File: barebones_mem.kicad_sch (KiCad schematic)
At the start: 0 parts

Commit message: routed the two 64Gb LPDDR4x RAM chips
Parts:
- added C128, C132: 47uF, Capacitor_SMD:C_0603_1608Metric, symbol Device:C
- added D15: TPD1E05U06DPYR, TPD1E05U06DPYR:DIO_TPD1E05U06DPYR, symbol TPD1E05U06DPYR:TPD1E05U06DPYR
- added Q4: MMBT3904, MMBT3904:P200_SOT-23, symbol MMBT3904:MMBT3904
- added R166, R167, R169: 10k, Resistor_SMD:R_0603_1608Metric, symbol Device:R
- added R168: 22R, Resistor_SMD:R_0603_1608Metric, symbol Device:R
- added TP5: RESETB, TestPoint:TestPoint_Pad_D1.5mm, symbol Connector:TestPoint
- added TP6: GND, TestPoint:TestPoint_Pad_D1.5mm, symbol Connector:TestPoint
- added U49: W25Q256JWEIQ, barebones:WSON-8_L8.0-W6.0-P1.27-TL-EP-1, symbol W25Q256JWEIQ:W25Q256JWEIQ_C2980994
- added U50: PCF85063ATL/1,118, barebones:10-DFN_2.6X2.6_, symbol PCF85063ATL_1_118:PCF85063ATL_1_118
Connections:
- new net: D15.2 (GND), Q4.1 (B), R169.2
- new net: R169.1, TP5.1
- new net: Q4.3 (C), R168.2
- new net FSPI-CLK: R168.1, U49.6 (CLK)
- new net FSPI-CS0: U49.1 (~{CS})
- new net FSPI-D0: U49.5 (DI(IO0))
- new net FSPI-D1: U49.2 (DO(IO1))
- new net FSPI-D2: R166.2, U49.3 (WP#(IO2))
- new net FSPI-D3: R167.2, U49.7 (~{HOLDor}/RESET#(IO3))
- new net GND: C128.1, C132.1, D15.1 (I/O), Q4.2 (E), U49.4 (GND), U49.9 (EP)
- new net VCC_1V8_S3: C128.2, C132.2, R166.1, R167.1, TP6.1, U49.8 (VCC)
- new net VSS: U50.11 (VSS), U50.5 (VSS)

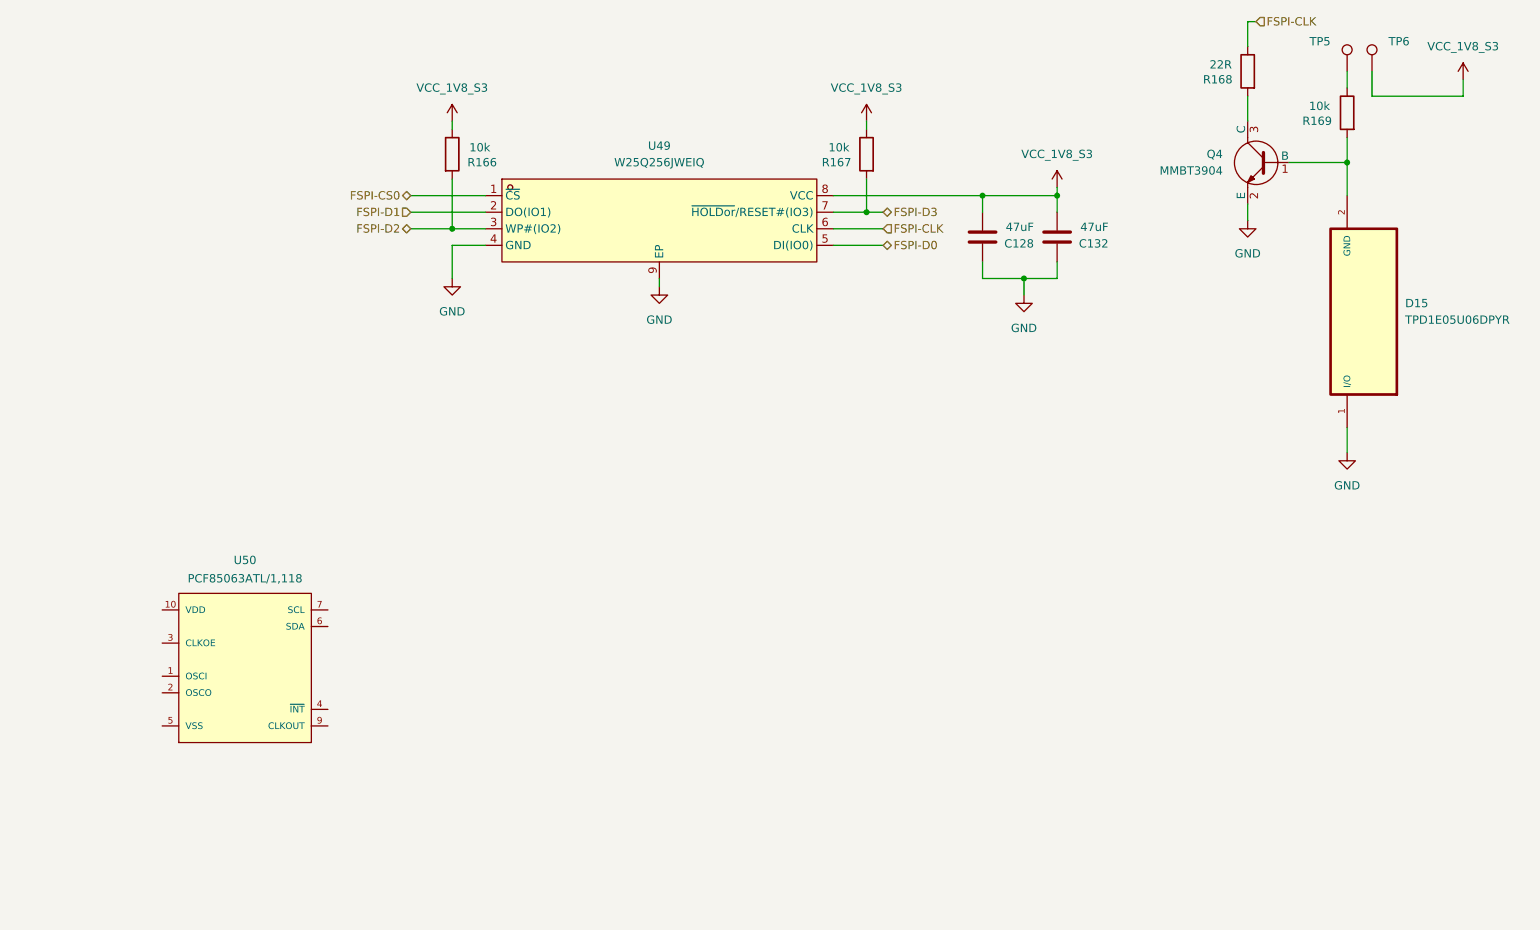
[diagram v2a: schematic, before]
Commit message: added the STM32L433RCT6 to act as the embedded controller
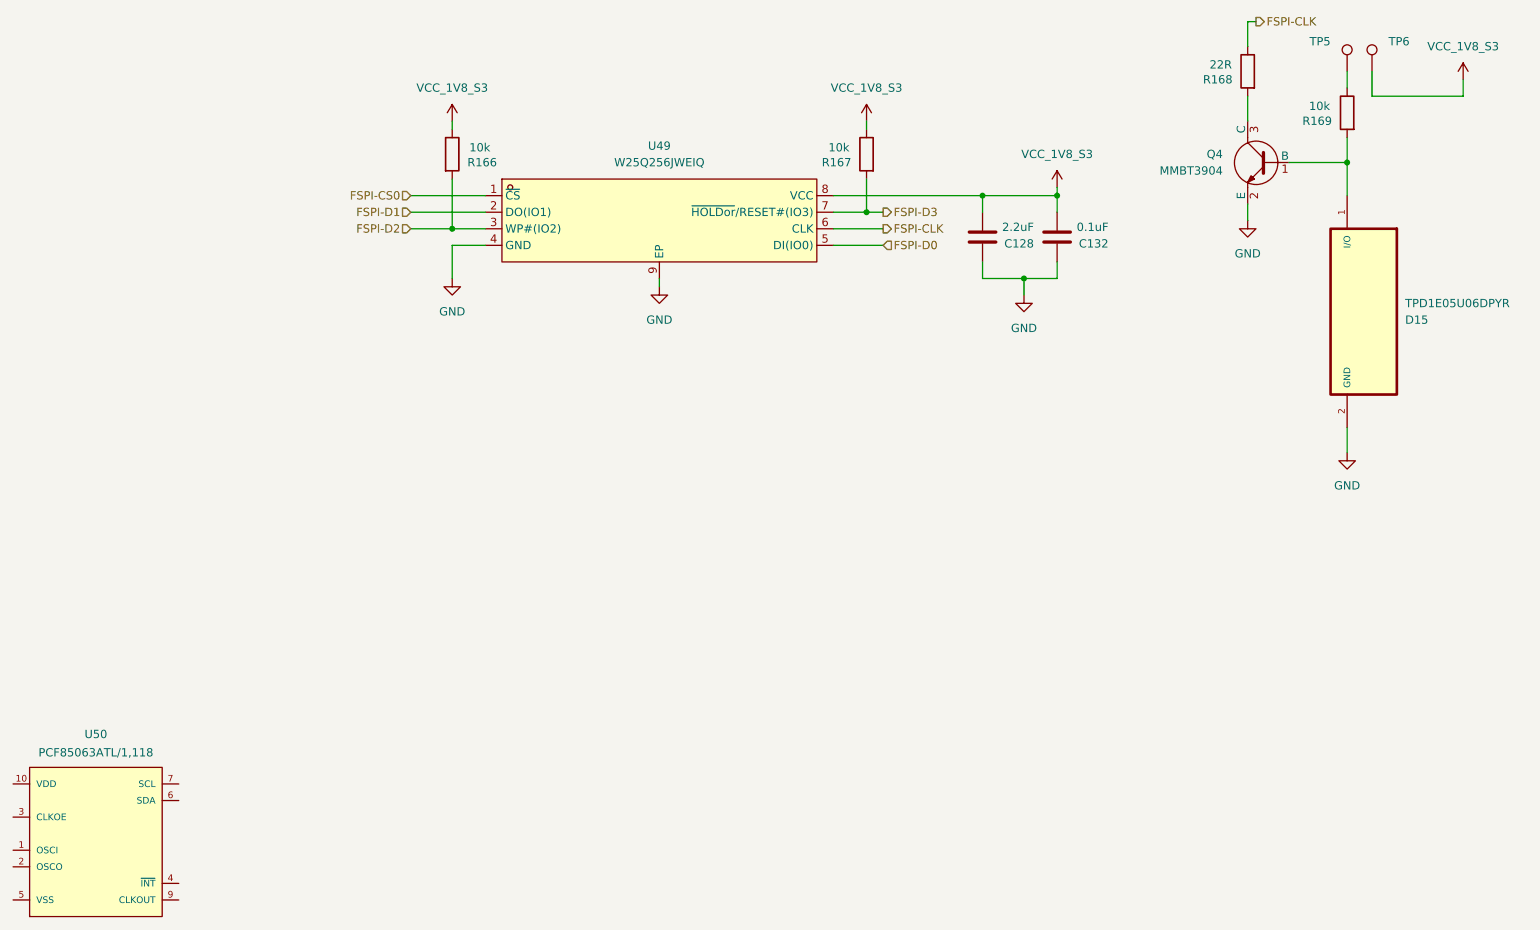
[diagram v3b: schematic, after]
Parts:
- C128: value 47uF -> 2.2uF
- C132: value 47uF -> 0.1uF
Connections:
- net GND: now also D15.2 (GND); no longer D15.1 (I/O)
- net at Q4.1 (B), R169.2: now also D15.1 (I/O); no longer D15.2 (GND)
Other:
- moved on the sheet: U50
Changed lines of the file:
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@@
 	)
 	(hierarchical_label "FSPI-CLK"
-		(shape input)
+		(shape output)
 		(at 184.15 53.34 0)
 		(effects
@@
 	)
 	(hierarchical_label "FSPI-D0"
-		(shape bidirectional)
+		(shape input)
 		(at 184.15 55.88 0)
 		(effects
@@
 	)
 	(hierarchical_label "FSPI-CLK"
-		(shape input)
+		(shape output)
 		(at 241.3 21.59 0)
 		(effects
@@
 	)
 	(hierarchical_label "FSPI-D3"
-		(shape bidirectional)
+		(shape output)
 		(at 184.15 50.8 0)
 		(effects
@@
 	)
 	(hierarchical_label "FSPI-CS0"
-		(shape bidirectional)
+		(shape input)
 		(at 111.76 48.26 180)
 		(effects
@@
 	)
 	(hierarchical_label "FSPI-D2"
-		(shape bidirectional)
+		(shape input)
 		(at 111.76 53.34 180)
 		(effects
@@
 		(lib_id "TPD1E05U06DPYR:TPD1E05U06DPYR")
 		(at 257.81 66.04 90)
-		(unit 1)
-		(body_style 1)
-		(exclude_from_sim no)
-		(in_bom yes)
-		(on_board yes)
-		(in_pos_files yes)
-		(dnp no)
-		(fields_autoplaced yes)
+		(mirror x)
+		(unit 1)
+		(body_style 1)
+		(exclude_from_sim no)
+		(in_bom yes)
+		(on_board yes)
+		(in_pos_files yes)
+		(dnp no)
 		(property "Reference" "D15"
-			(at 264.16 64.7699 90)
+			(at 264.16 67.3101 90)
 			(show_name no)
 			(do_not_autoplace no)
@@
 		)
 		(property "Value" "TPD1E05U06DPYR"
-			(at 264.16 67.3099 90)
+			(at 264.16 64.7701 90)
 			(show_name no)
 			(do_not_autoplace no)
@@
 			)
 		)
-		(property "Value" "47uF"
+		(property "Value" "2.2uF"
 			(at 207.264 53.086 0)
 			(show_name no)
@@
 			)
 		)
-		(property "Value" "47uF"
+		(property "Value" "0.1uF"
 			(at 218.694 53.086 0)
 			(show_name no)
@@
 	(symbol
 		(lib_id "PCF85063ATL_1_118:PCF85063ATL_1_118")
-		(at 86.36 119.38 0)
+		(at 63.5 146.05 0)
 		(unit 1)
 		(body_style 1)
@@
 		(dnp no)
 		(property "Reference" "U50"
-			(at 86.36 104.14 0)
+			(at 63.5 130.81 0)
 			(show_name no)
 			(do_not_autoplace no)
@@
 		)
 		(property "Value" "PCF85063ATL/1,118"
-			(at 86.36 107.696 0)
+			(at 63.5 134.366 0)
 			(show_name no)
 			(do_not_autoplace no)
@@
 		)
 		(property "Footprint" "barebones:10-DFN_2.6X2.6_"
-			(at 86.36 119.38 0)
+			(at 63.5 146.05 0)
 			(hide yes)
 			(show_name no)
@@
 		)
 		(property "Datasheet" ""
-			(at 86.36 119.38 0)
+			(at 63.5 146.05 0)
 			(hide yes)
 			(show_name no)
@@
 		)
 		(property "Description" "Real Time Clock (RTC) IC Clock/Calendar - I²C, 2-Wire Serial 10-XFDFN Exposed Pad"
-			(at 86.36 119.38 0)
+			(at 63.5 146.05 0)
 			(hide yes)
 			(show_name no)
@@
 		)
 		(property "MF" "NXP USA"
-			(at 86.36 119.38 0)
+			(at 63.5 146.05 0)
 			(hide yes)
 			(show_name no)
@@
 		)
 		(property "Package" "DFN-10 NXP Semiconductors"
-			(at 86.36 119.38 0)
+			(at 63.5 146.05 0)
 			(hide yes)
 			(show_name no)
@@
 		)
 		(property "Price" "None"
-			(at 86.36 119.38 0)
+			(at 63.5 146.05 0)
 			(hide yes)
 			(show_name no)
@@
 		)
 		(property "Check_prices" "https://www.snapeda.com/parts/PCF85063ATL/1,118/NXP+Semiconductors/view-part/?ref=eda"
-			(at 86.36 119.38 0)
+			(at 63.5 146.05 0)
 			(hide yes)
 			(show_name no)
@@
 		)
 		(property "SnapEDA_Link" "https://www.snapeda.com/parts/PCF85063ATL/1,118/NXP+Semiconductors/view-part/?ref=snap"
-			(at 86.36 119.38 0)
+			(at 63.5 146.05 0)
 			(hide yes)
 			(show_name no)
@@
 		)
 		(property "PROD_ID" "IC-15415"
-			(at 86.36 119.38 0)
+			(at 63.5 146.05 0)
 			(hide yes)
 			(show_name no)
@@
 		)
 		(property "Availability" "In Stock"
-			(at 86.36 119.38 0)
+			(at 63.5 146.05 0)
 			(hide yes)
 			(show_name no)
@@
 		)
 		(property "MP" "PCF85063ATL/1,118"
-			(at 86.36 119.38 0)
-			(hide yes)
-			(show_name no)
+			(at 63.5 146.05 0)
+			(hide yes)
+			(show_name no)

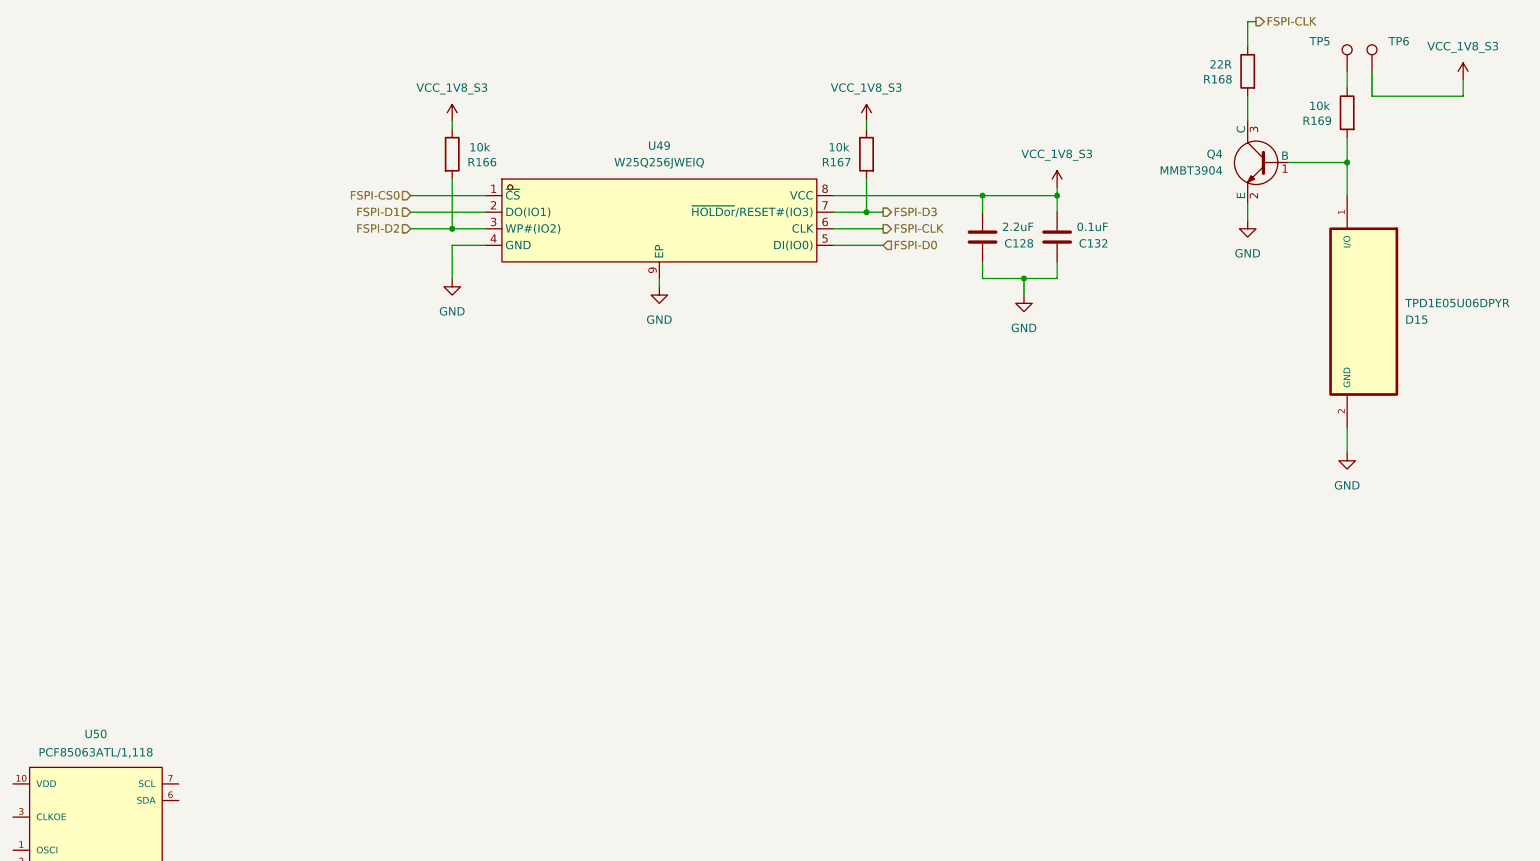
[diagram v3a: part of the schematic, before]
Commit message: added the display connector and its 12V power supply
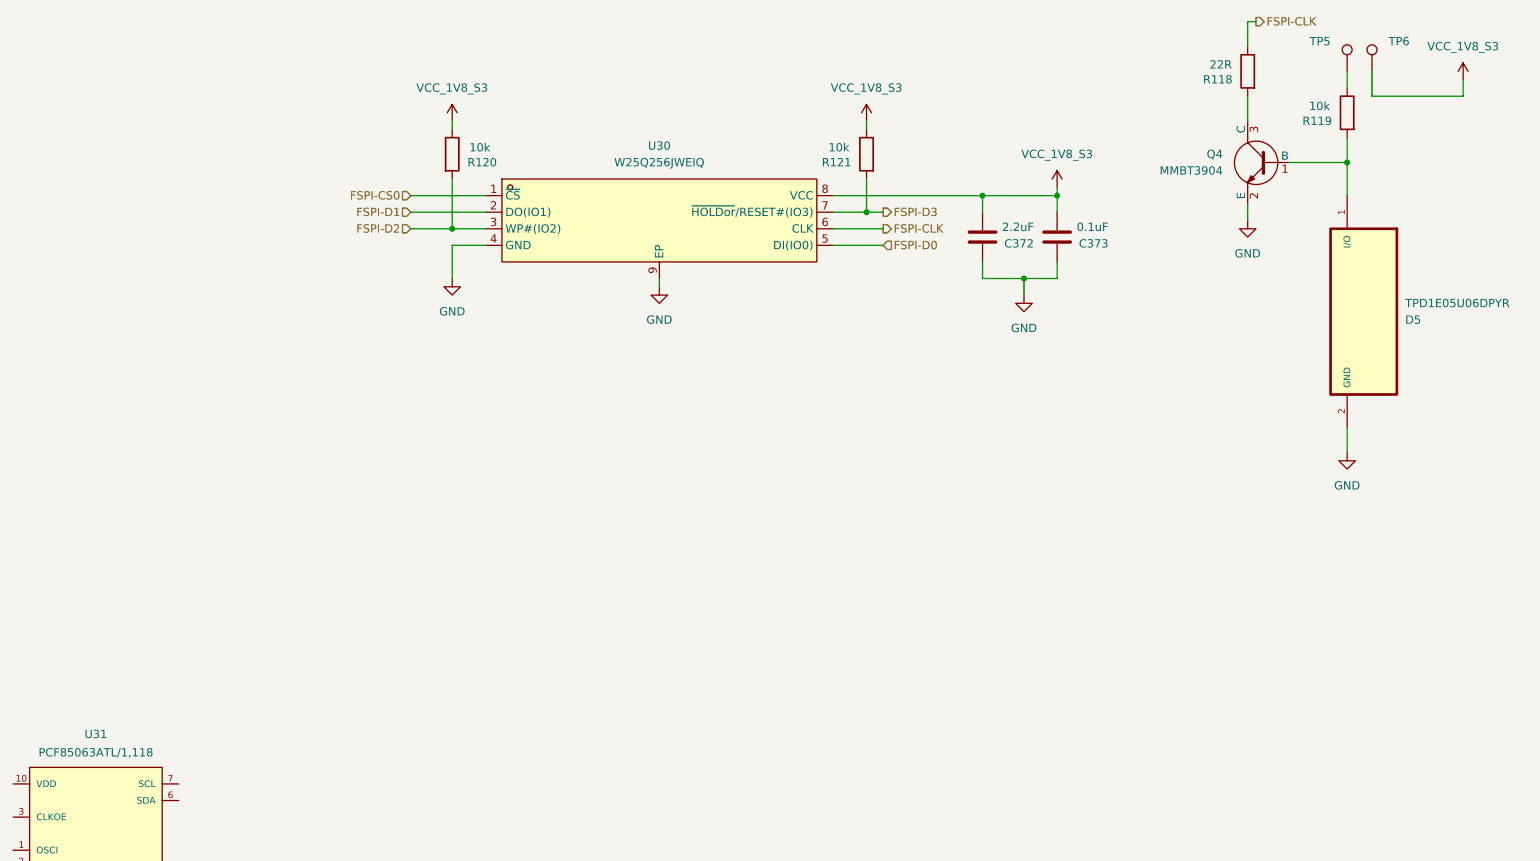
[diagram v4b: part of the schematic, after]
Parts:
- renumbered C128 to C372, C132 to C373, D15 to D5, R168 to R118, R169 to R119, R166 to R120, R167 to R121, U49 to U30, U50 to U31
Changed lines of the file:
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@@
 		(dnp no)
 		(fields_autoplaced yes)
-		(property "Reference" "#PWR0389"
+		(property "Reference" "#PWR0334"
 			(at 118.11 67.31 0)
 			(hide yes)
@@
 			(project "barebones"
 				(path "/55e8bb80-206a-472b-ac89-6555b6c3d282/10a7f033-abc9-48da-a7a0-2d26902a94e5"
-					(reference "#PWR0389")
+					(reference "#PWR0334")
 					(unit 1)
 				)
@@
 		(dnp no)
 		(fields_autoplaced yes)
-		(property "Reference" "#PWR0394"
+		(property "Reference" "#PWR0329"
 			(at 273.05 34.29 0)
 			(hide yes)
@@
 			(project "barebones"
 				(path "/55e8bb80-206a-472b-ac89-6555b6c3d282/10a7f033-abc9-48da-a7a0-2d26902a94e5"
-					(reference "#PWR0394")
+					(reference "#PWR0329")
 					(unit 1)
 				)
@@
 		(in_pos_files yes)
 		(dnp no)
-		(property "Reference" "D15"
+		(property "Reference" "D5"
 			(at 264.16 67.3101 90)
 			(show_name no)
@@
 			(project "barebones"
 				(path "/55e8bb80-206a-472b-ac89-6555b6c3d282/10a7f033-abc9-48da-a7a0-2d26902a94e5"
-					(reference "D15")
+					(reference "D5")
 					(unit 1)
 				)
@@
 		(in_pos_files yes)
 		(dnp no)
-		(property "Reference" "R169"
+		(property "Reference" "R119"
 			(at 248.412 36.83 0)
 			(show_name no)
@@
 			(project "barebones"
 				(path "/55e8bb80-206a-472b-ac89-6555b6c3d282/10a7f033-abc9-48da-a7a0-2d26902a94e5"
-					(reference "R169")
+					(reference "R119")
 					(unit 1)
 				)
@@
 		(in_pos_files yes)
 		(dnp no)
-		(property "Reference" "C128"
+		(property "Reference" "C372"
 			(at 207.264 55.626 0)
 			(show_name no)
@@
 			(project "barebones"
 				(path "/55e8bb80-206a-472b-ac89-6555b6c3d282/10a7f033-abc9-48da-a7a0-2d26902a94e5"
-					(reference "C128")
+					(reference "C372")
 					(unit 1)
 				)
@@
 		(dnp no)
 		(fields_autoplaced yes)
-		(property "Reference" "#PWR0391"
+		(property "Reference" "#PWR0336"
 			(at 205.74 69.85 0)
 			(hide yes)
@@
 			(project "barebones"
 				(path "/55e8bb80-206a-472b-ac89-6555b6c3d282/10a7f033-abc9-48da-a7a0-2d26902a94e5"
-					(reference "#PWR0391")
+					(reference "#PWR0336")
 					(unit 1)
 				)
@@
 		(dnp no)
 		(fields_autoplaced yes)
-		(property "Reference" "#PWR0387"
+		(property "Reference" "#PWR0332"
 			(at 210.82 50.8 0)
 			(hide yes)
@@
 			(project "barebones"
 				(path "/55e8bb80-206a-472b-ac89-6555b6c3d282/10a7f033-abc9-48da-a7a0-2d26902a94e5"
-					(reference "#PWR0387")
+					(reference "#PWR0332")
 					(unit 1)
 				)
@@
 		(in_pos_files yes)
 		(dnp no)
-		(property "Reference" "C132"
+		(property "Reference" "C373"
 			(at 218.694 55.626 0)
 			(show_name no)
@@
 			(project "barebones"
 				(path "/55e8bb80-206a-472b-ac89-6555b6c3d282/10a7f033-abc9-48da-a7a0-2d26902a94e5"
-					(reference "C132")
+					(reference "C373")
 					(unit 1)
 				)
@@
 		(dnp no)
 		(fields_autoplaced yes)
-		(property "Reference" "#PWR0393"
+		(property "Reference" "#PWR0333"
 			(at 240.03 58.42 0)
 			(hide yes)
@@
 			(project "barebones"
 				(path "/55e8bb80-206a-472b-ac89-6555b6c3d282/10a7f033-abc9-48da-a7a0-2d26902a94e5"
-					(reference "#PWR0393")
+					(reference "#PWR0333")
 					(unit 1)
 				)
@@
 		(dnp no)
 		(fields_autoplaced yes)
-		(property "Reference" "#PWR0386"
+		(property "Reference" "#PWR0330"
 			(at 118.11 40.64 0)
 			(hide yes)
@@
 			(project "barebones"
 				(path "/55e8bb80-206a-472b-ac89-6555b6c3d282/10a7f033-abc9-48da-a7a0-2d26902a94e5"
-					(reference "#PWR0386")
+					(reference "#PWR0330")
 					(unit 1)
 				)
@@
 		(in_pos_files yes)
 		(dnp no)
-		(property "Reference" "R168"
+		(property "Reference" "R118"
 			(at 233.172 30.48 0)
 			(show_name no)
@@
 			(project "barebones"
 				(path "/55e8bb80-206a-472b-ac89-6555b6c3d282/10a7f033-abc9-48da-a7a0-2d26902a94e5"
-					(reference "R168")
+					(reference "R118")
 					(unit 1)
 				)
@@
 		(dnp no)
 		(fields_autoplaced yes)
-		(property "Reference" "U49"
+		(property "Reference" "U30"
 			(at 149.86 40.64 0)
 			(show_name no)
@@
 			(project "barebones"
 				(path "/55e8bb80-206a-472b-ac89-6555b6c3d282/10a7f033-abc9-48da-a7a0-2d26902a94e5"
-					(reference "U49")
+					(reference "U30")
 					(unit 1)
 				)
@@
 		(dnp no)
 		(fields_autoplaced yes)
-		(property "Reference" "#PWR0392"
+		(property "Reference" "#PWR0337"
 			(at 255.27 93.98 0)
 			(hide yes)
@@
 			(project "barebones"
 				(path "/55e8bb80-206a-472b-ac89-6555b6c3d282/10a7f033-abc9-48da-a7a0-2d26902a94e5"
-					(reference "#PWR0392")
+					(reference "#PWR0337")
 					(unit 1)
 				)
@@
 		(in_pos_files yes)
 		(dnp no)
-		(property "Reference" "R167"
+		(property "Reference" "R121"
 			(at 174.752 43.18 0)
 			(show_name no)
@@
 			(project "barebones"
 				(path "/55e8bb80-206a-472b-ac89-6555b6c3d282/10a7f033-abc9-48da-a7a0-2d26902a94e5"
-					(reference "R167")
+					(reference "R121")
 					(unit 1)
 				)
@@
 		(dnp no)
 		(fields_autoplaced yes)
-		(property "Reference" "#PWR0390"
+		(property "Reference" "#PWR0335"
 			(at 149.86 68.58 0)
 			(hide yes)
@@
 			(project "barebones"
 				(path "/55e8bb80-206a-472b-ac89-6555b6c3d282/10a7f033-abc9-48da-a7a0-2d26902a94e5"
-					(reference "#PWR0390")
+					(reference "#PWR0335")
 					(unit 1)
 				)
@@
 		(in_pos_files yes)
 		(dnp no)
-		(property "Reference" "R166"
+		(property "Reference" "R120"
 			(at 124.968 43.18 0)
 			(show_name no)
@@
 			(project "barebones"
 				(path "/55e8bb80-206a-472b-ac89-6555b6c3d282/10a7f033-abc9-48da-a7a0-2d26902a94e5"
-					(reference "R166")
+					(reference "R120")
 					(unit 1)
 				)
@@
 		(dnp no)
 		(fields_autoplaced yes)
-		(property "Reference" "#PWR0388"
+		(property "Reference" "#PWR0331"
 			(at 181.61 40.64 0)
 			(hide yes)
@@
 			(project "barebones"
 				(path "/55e8bb80-206a-472b-ac89-6555b6c3d282/10a7f033-abc9-48da-a7a0-2d26902a94e5"
-					(reference "#PWR0388")
+					(reference "#PWR0331")
 					(unit 1)
 				)
@@
 		(in_pos_files yes)
 		(dnp no)
-		(property "Reference" "U50"
+		(property "Reference" "U31"
 			(at 63.5 130.81 0)
 			(show_name no)
@@
 			(project "barebones"
 				(path "/55e8bb80-206a-472b-ac89-6555b6c3d282/10a7f033-abc9-48da-a7a0-2d26902a94e5"
-					(reference "U50")
-					(unit 1)
-				)
+					(reference "U31")
+					(unit 1)
+				)
